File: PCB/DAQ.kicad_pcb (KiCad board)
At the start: 2 copper layers, 6 parts, among them J1 Arduino_Mega_Header, U1 SDshield, U2 RTC, U3 ADC, U4 NOKIA5110, U5 DAC

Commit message: PCB Improvement
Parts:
- added J2: Conn_01x07, Pin_Headers:Pin_Header_Straight_1x07_Pitch2.54mm, F.Cu at (51.7, 27.8)
- added J3: Conn_01x08, Pin_Headers:Pin_Header_Straight_1x08_Pitch2.54mm, F.Cu at (71.9, 27.9)
- added J5: Conn_02x18_Counter_Clockwise, Pin_Headers:Pin_Header_Straight_2x18_Pitch2.54mm, B.Cu at (115.1, 76.1)
- added J6: Conn_01x10, Pin_Headers:Pin_Header_Straight_1x10_Pitch2.54mm, F.Cu at (40.0, 76.2)
- added J7: Conn_01x08, Pin_Headers:Pin_Header_Straight_1x08_Pitch2.54mm, F.Cu at (66.9, 76.1)
- added J8: Conn_01x07, Pin_Headers:Pin_Header_Straight_1x07_Pitch2.54mm, F.Cu at (92.3, 76.2)
- J1, U2: moved to B.Cu
- moved U5 147.7 mm to (35.3, 126.6)
- moved U4 95.8 mm to (65.5, 100.2)
- moved U3 86.6 mm to (26.4, 100.2)
- moved U2 84.3 mm to (128.9, 78.0)
- moved U1 42.0 mm to (127.1, 28.0)
- moved J1 4.92 mm to (70.7, 52.0)

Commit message: PCB Improvements
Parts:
- added C1: 100uF, Capacitors_THT:CP_Axial_L11.0mm_D6.0mm_P18.00mm_Horizontal, F.Cu at (164.2, 112.4)
- added C2: 0.1uF, Capacitors_THT:CP_Axial_L11.0mm_D6.0mm_P18.00mm_Horizontal, F.Cu at (114.6, 113.2)
- added C3: 10uF, Capacitors_THT:CP_Axial_L11.0mm_D6.0mm_P18.00mm_Horizontal, F.Cu at (114.4, 120.6)
- added C4: 1uF, Capacitors_THT:CP_Axial_L11.0mm_D6.0mm_P18.00mm_Horizontal, F.Cu at (114.4, 128.4)
- added CC+1: 0.01uF, Capacitors_THT:CP_Axial_L11.0mm_D6.0mm_P18.00mm_Horizontal, F.Cu at (132.4, 105.0)
- added CC-1: 0.01uF, Capacitors_THT:CP_Axial_L11.0mm_D6.0mm_P18.00mm_Horizontal, F.Cu at (132.4, 135.8)
- added CF+1: 100uF, Capacitors_THT:CP_Axial_L11.0mm_D6.0mm_P18.00mm_Horizontal, F.Cu at (172.6, 105.4)
- added CF-1: 100uF, Capacitors_THT:CP_Axial_L11.0mm_D6.0mm_P18.00mm_Horizontal, F.Cu at (178.4, 136.6)
- added DX+1: D_Schottky, Diodes_THT:D_A-405_P12.70mm_Horizontal, F.Cu at (165.6, 107.0)
- added DX-1: D_Schottky, Diodes_THT:D_A-405_P12.70mm_Horizontal, F.Cu at (158.2, 135.6)
- added IC1: MAX743CWE+, Housings_DIP:DIP-16_W7.62mm, F.Cu at (138.0, 104.6)
- added J4: Conn_01x08, Pin_Headers:Pin_Header_Straight_1x08_Pitch2.54mm, F.Cu at (94.8, 27.8)
- added LX+1: 100uH, Inductors_THT:L_Axial_L9.5mm_D4.0mm_P12.70mm_Horizontal_Fastron_SMCC, F.Cu at (152.8, 87.6)
- added LX-1: 100uH, Inductors_THT:L_Axial_L9.5mm_D4.0mm_P12.70mm_Horizontal_Fastron_SMCC, F.Cu at (152.6, 136.0)
- moved U4 19.6 mm to (54.8, 83.8)
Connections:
- U4 pad 1: /PIN2 -> /PIN7
- U4 pad 2: /PIN3 -> /PIN6
- U4 pad 4: /PIN6 -> /PIN3
- U4 pad 5: /PIN7 -> /PIN2
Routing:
- net /5V: track 0.00 -> 258.3 mm
- net /GND: track 0.00 -> 144.5 mm
- net /3.3V: track 0.00 -> 93.3 mm
- net /PIN4: track 0.00 -> 80.9 mm
- net Net-(C2-Pad1): track 0.00 -> 55.3 mm
- net /SCL: track 0.00 -> 54.8 mm
- net /SDA: track 0.00 -> 52.6 mm
- net /+15V: track 0.00 -> 30.0 mm
- net Net-(DX-1-Pad1): track 0.00 -> 26.4 mm
- net Net-(CC-1-Pad1): track 0.00 -> 15.7 mm
- net Net-(DX+1-Pad2): track 0.00 -> 14.1 mm
- net /PIN35: track 0.00 -> 13.6 mm
- net /PIN31: track 0.00 -> 13.6 mm
- net /PIN33: track 0.00 -> 13.6 mm
- net /PIN6: track 0.00 -> 13.5 mm
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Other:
- net class Default: trace_width 0.25 -> 1

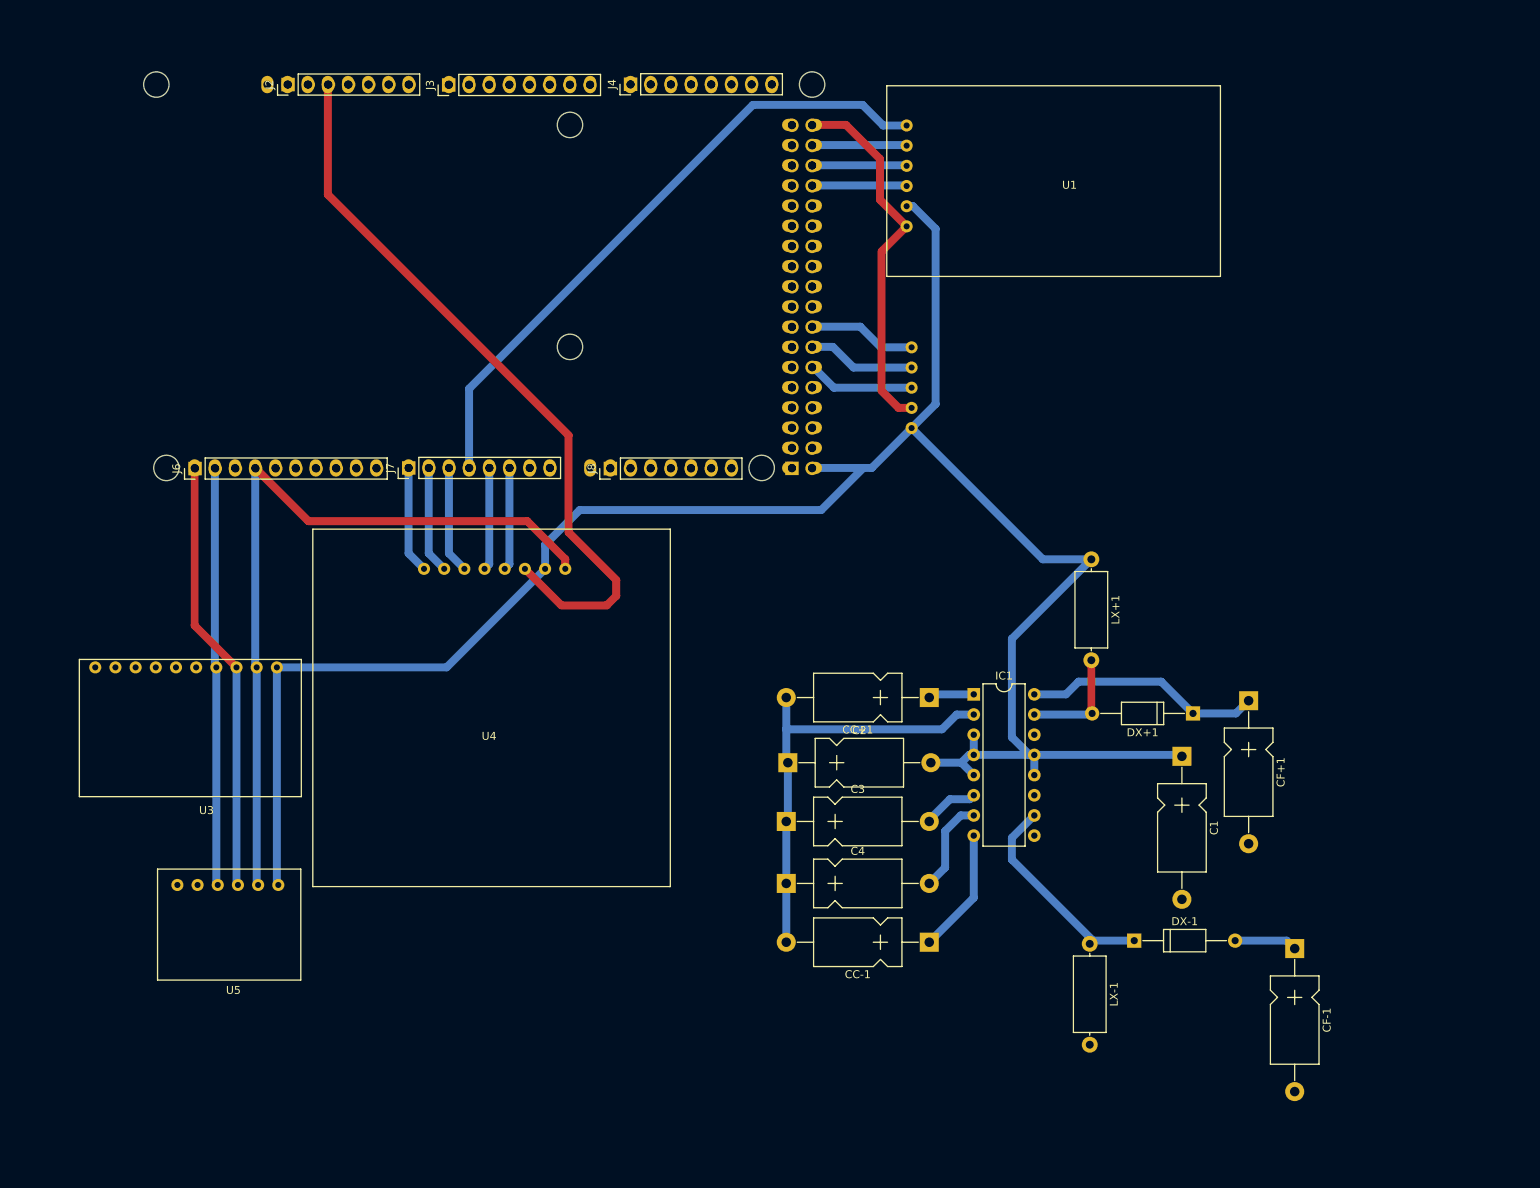
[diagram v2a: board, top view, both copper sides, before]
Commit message: Add ground plane,max743 and started analogic conditioner
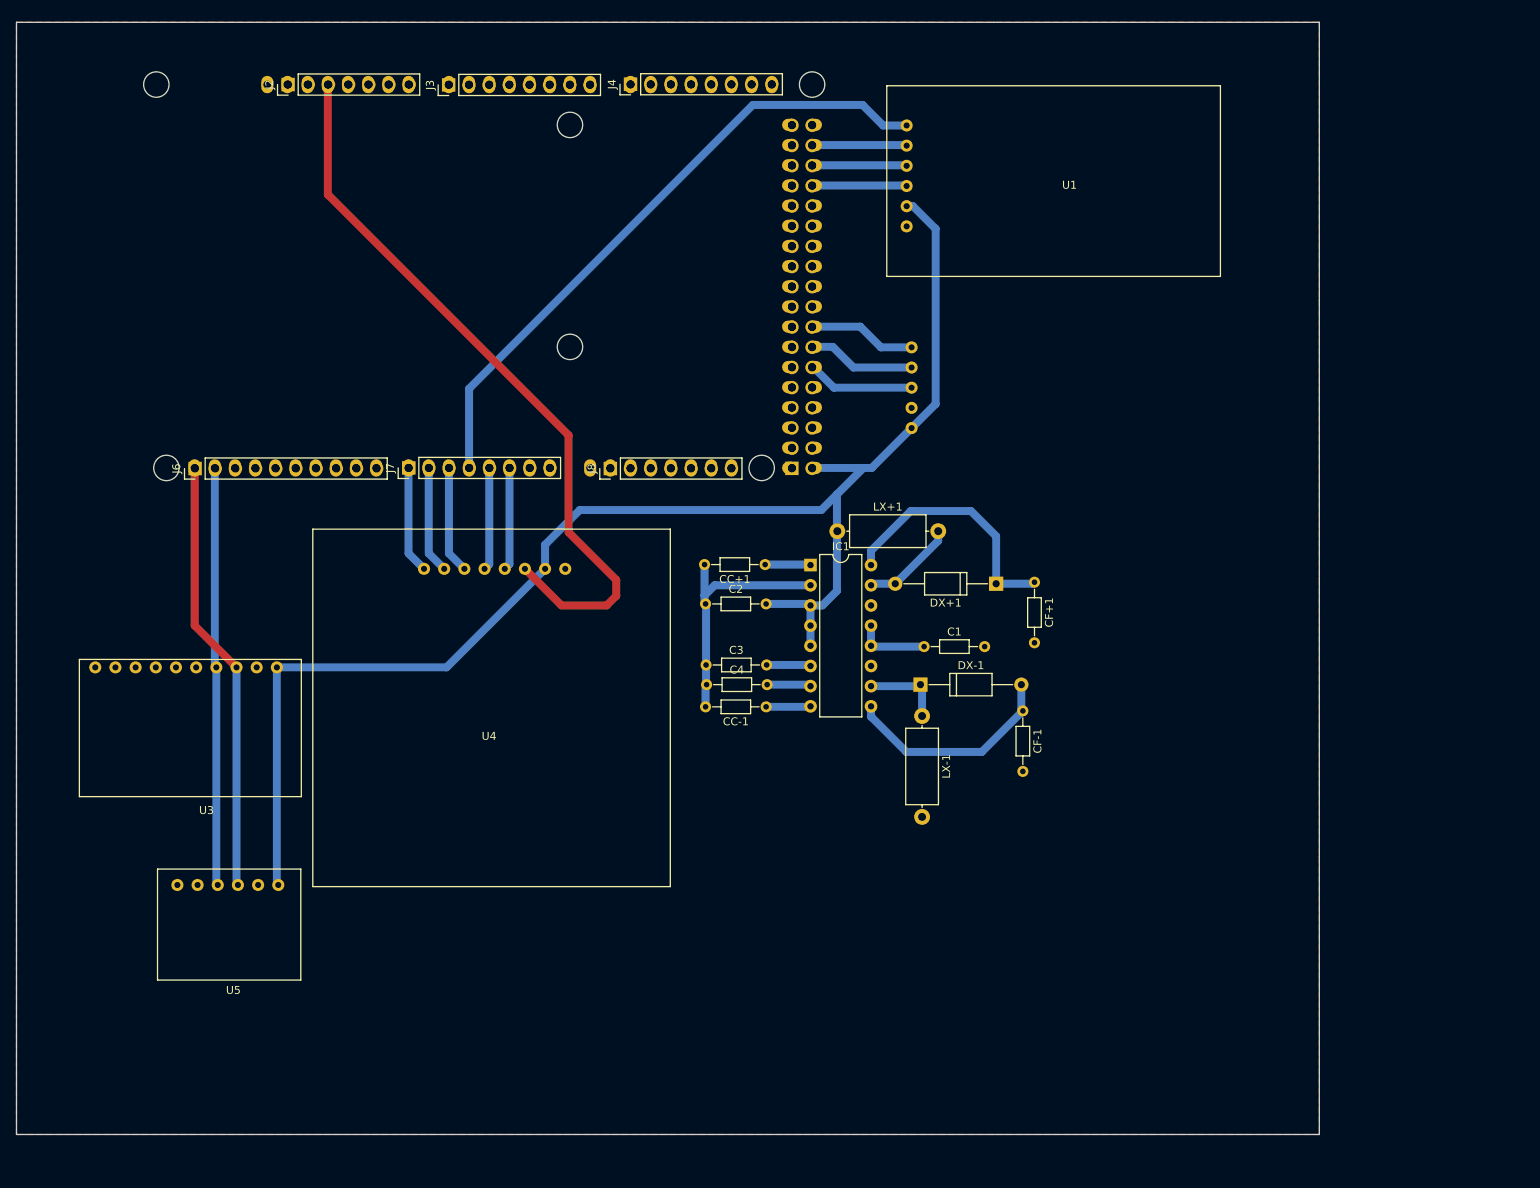
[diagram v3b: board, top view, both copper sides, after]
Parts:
- C1, C2, C3, C4, CC+1, CC-1, CF+1, CF-1: footprint Capacitors_THT:CP_Axial_L11.0mm_D6.0mm_P18.00mm_Horizontal -> Resistors_THT:R_Axial_DIN0204_L3.6mm_D1.6mm_P7.62mm_Horizontal
- moved CF-1 45.5 mm to (144.2, 106.7)
- moved DX-1 42.0 mm to (131.3, 103.4)
- moved CC-1 36.1 mm to (111.9, 106.2)
- moved LX-1 35.6 mm to (131.5, 107.3)
- moved C1 35.3 mm to (131.7, 98.6), turned to 0 degrees
- moved LX+1 32.2 mm to (120.8, 84.1), turned to 0 degrees
- moved CF+1 30.8 mm to (145.6, 90.5)
- moved DX+1 29.7 mm to (140.8, 90.7)
- moved C4 27.0 mm to (104.4, 103.4)
- moved CC+1 26.6 mm to (111.7, 88.3)
- moved IC1 26.2 mm to (117.4, 88.3)
- moved C2 22.5 mm to (104.2, 93.2)
- moved C3 22.1 mm to (104.3, 100.9)
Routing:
- net /GND: track 144.5 -> 0.52 mm
- net /5V: track 258.3 -> 196.1 mm
- net Net-(C2-Pad1): track 55.3 -> 31.9 mm
- net /-15V: track 7.91 -> 27.8 mm
- net Net-(DX-1-Pad1): track 26.4 -> 10.3 mm
- net Net-(CC-1-Pad1): track 15.7 -> 5.61 mm
- net Net-(C4-Pad2): track 11.8 -> 5.54 mm
- net Net-(DX+1-Pad2): track 14.1 -> 12.0 mm
- net /+15V: track 30.0 -> 31.8 mm
- net Net-(C3-Pad2): track 7.08 -> 5.58 mm
- added copper zone on F.Cu, net /GND
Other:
- board outline added: 164 x 140 mm

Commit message: Analog Conditioner added int PCB layout
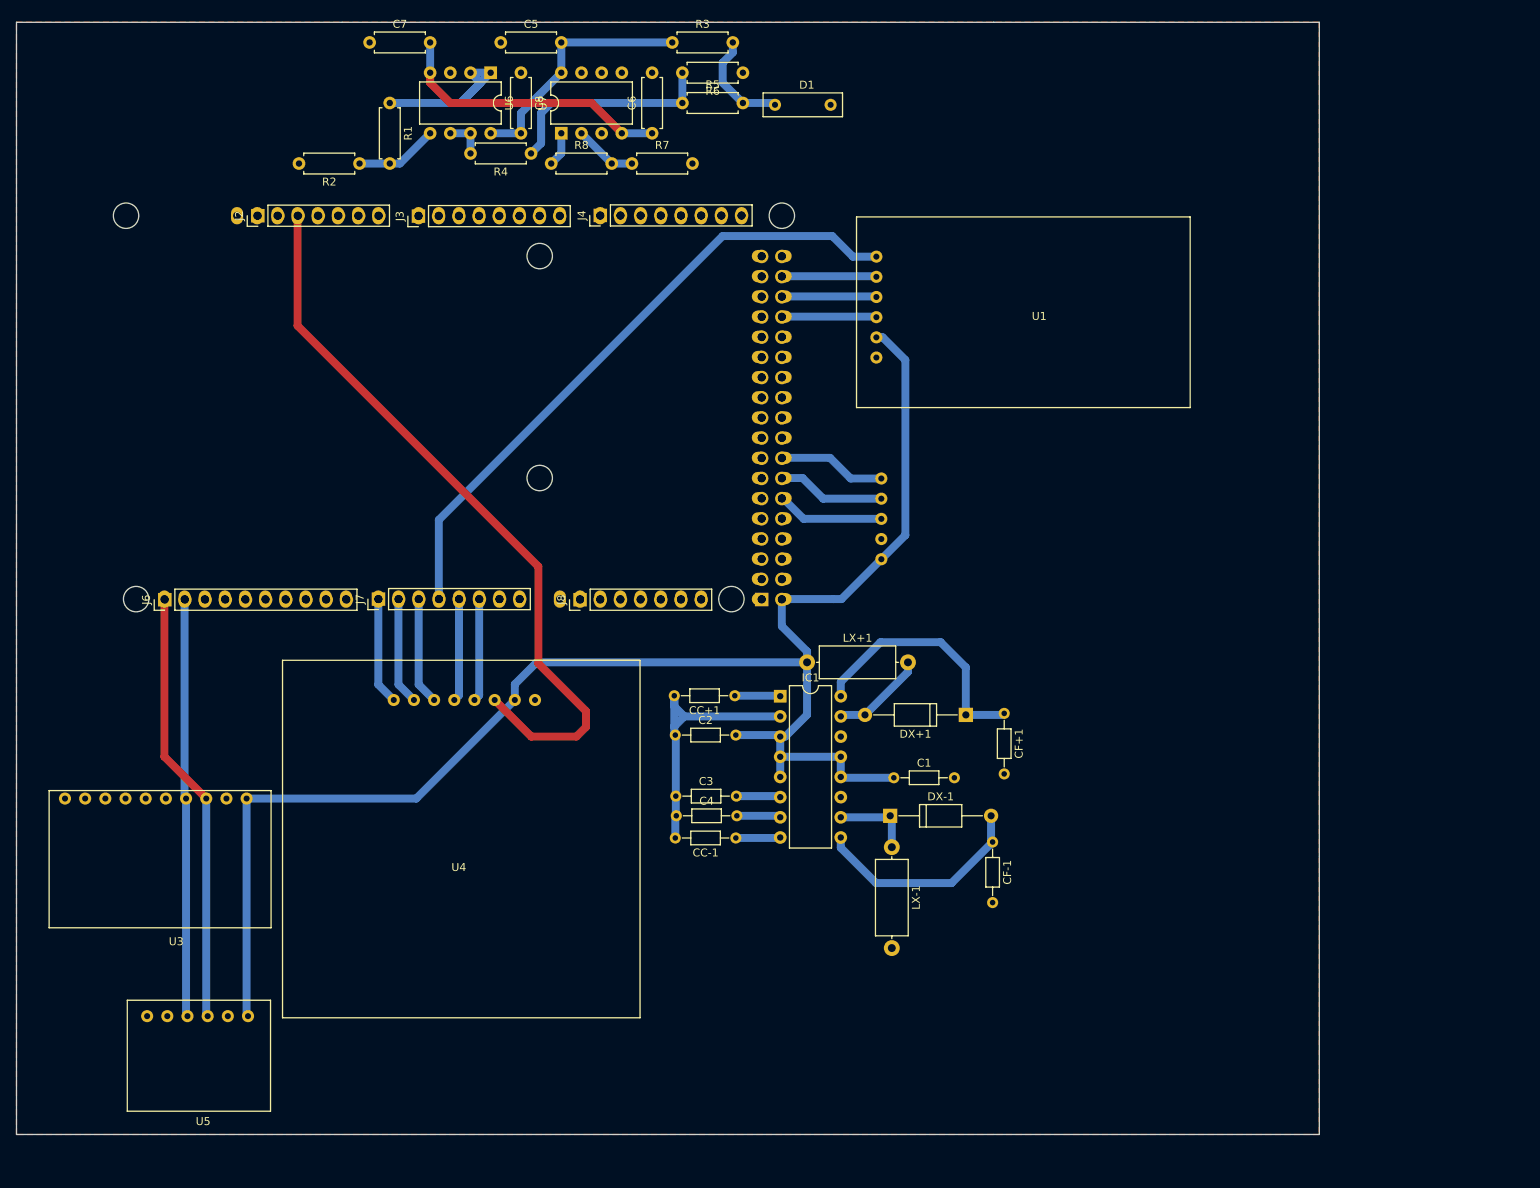
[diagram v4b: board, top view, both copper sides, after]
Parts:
- added C5: 100nF, Resistors_THT:R_Axial_DIN0207_L6.3mm_D2.5mm_P7.62mm_Horizontal, F.Cu at (78.5, 22.5)
- added C6: 100nF, Resistors_THT:R_Axial_DIN0207_L6.3mm_D2.5mm_P7.62mm_Horizontal, F.Cu at (97.5, 34.0)
- added C7: 100nF, Resistors_THT:R_Axial_DIN0207_L6.3mm_D2.5mm_P7.62mm_Horizontal, F.Cu at (62.0, 22.5)
- added C8: 100nF, Resistors_THT:R_Axial_DIN0207_L6.3mm_D2.5mm_P7.62mm_Horizontal, F.Cu at (81.0, 26.4)
- added D1: LM4040, TH-R:R-C-L-D, F.Cu at (111.5, 28.9)
- added R1: 68k, Resistors_THT:R_Axial_DIN0207_L6.3mm_D2.5mm_P7.62mm_Horizontal, F.Cu at (64.5, 30.2)
- added R2: 18k, Resistors_THT:R_Axial_DIN0207_L6.3mm_D2.5mm_P7.62mm_Horizontal, F.Cu at (60.7, 37.8)
- added R3: 22k, Resistors_THT:R_Axial_DIN0207_L6.3mm_D2.5mm_P7.62mm_Horizontal, F.Cu at (100.0, 22.5)
- added R4: 100k, Resistors_THT:R_Axial_DIN0207_L6.3mm_D2.5mm_P7.62mm_Horizontal, F.Cu at (82.3, 36.5)
- added R5: 200k, Resistors_THT:R_Axial_DIN0207_L6.3mm_D2.5mm_P7.62mm_Horizontal, F.Cu at (101.3, 30.2)
- added R6: 51k, Resistors_THT:R_Axial_DIN0207_L6.3mm_D2.5mm_P7.62mm_Horizontal, F.Cu at (108.9, 26.4)
- added R7: 47, Resistors_THT:R_Axial_DIN0207_L6.3mm_D2.5mm_P7.62mm_Horizontal, F.Cu at (95.0, 37.8)
- added R8: 100k, Resistors_THT:R_Axial_DIN0207_L6.3mm_D2.5mm_P7.62mm_Horizontal, F.Cu at (84.8, 37.8)
- added U6: LM358, Housings_DIP:DIP-8_W7.62mm, F.Cu at (77.2, 26.4)
- added U7: LM358, Housings_DIP:DIP-8_W7.62mm, F.Cu at (86.1, 34.0)
- moved LX-1 16.9 mm to (127.7, 123.8)
- moved C1 16.9 mm to (127.9, 115.1)
- moved C3 16.9 mm to (100.5, 117.4)
- moved CC-1 16.9 mm to (108.1, 122.7)
- moved CF+1 16.9 mm to (141.8, 107.0)
- moved CF-1 16.9 mm to (140.4, 123.2)
- moved DX+1 16.9 mm to (137.0, 107.2)
- moved IC1 16.9 mm to (113.6, 104.8)
- moved J7 16.9 mm to (63.1, 92.6)
- moved U2 16.9 mm to (125.1, 94.5)
- moved U5 16.9 mm to (31.4, 143.1)
- moved J3 16.9 mm to (68.1, 44.4)
- moved J4 16.9 mm to (91.0, 44.3)
- moved J5 16.9 mm to (111.3, 92.7)
- moved J6 16.9 mm to (36.2, 92.7)
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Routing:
- net /-15V: track 27.8 -> 63.4 mm
- net /15V: track 0.00 -> 31.3 mm
- net Net-(R4-Pad1): track 0.00 -> 27.7 mm
- net Net-(R1-Pad1): track 0.00 -> 22.2 mm
- net Net-(D1-Pad1): track 0.00 -> 13.3 mm
- net Net-(R1-Pad2): track 0.00 -> 10.5 mm
- net Net-(R7-Pad1): track 0.00 -> 7.93 mm
- net Net-(R4-Pad2): track 0.00 -> 5.08 mm
- net /5V: track 196.1 -> 200.7 mm
- net Net-(R8-Pad1): track 0.00 -> 4.34 mm
- net Net-(C2-Pad1): track 31.9 -> 35.0 mm

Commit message: Changed RTC module on PCB
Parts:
- U2: footprint RTC:SDShield -> SDShield:SDShield; moved to F.Cu
- U4: moved to B.Cu
- moved U4 45.4 mm to (96.2, 103.8), turned to 180 degrees
- moved U2 25.1 mm to (122.9, 69.5)
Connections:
- J1 pad 26: Net-(J1-Pad26) -> /PIN52
- J1 pad 27: Net-(J1-Pad27) -> /PIN50
- J1 pad 43: /GND -> Net-(J1-Pad43)
- J1 pad 44: /PIN52 -> /PIN53
- J1 pad 46: /PIN50 -> Net-(J1-Pad46)
- J1 pad 71: /PIN2 -> Net-(J1-Pad71)
- J8 pad 6: Net-(J8-Pad6) -> /SDA
- J8 pad 7: Net-(J8-Pad7) -> /SCL
- U1 pad 1: /PIN4 -> /PIN53
- U2 pad 1: /5V -> /GND
- U2 pad 2: /GND -> /5V
- U2 pad 3: /PIN31 -> /SDA
- U2 pad 4: /PIN33 -> /SCL
- U2 pad 5: /PIN35 -> (no net)
- U4 pad 1: /PIN7 -> /PIN3
- U4 pad 2: /PIN6 -> /PIN4
- U4 pad 4: /PIN3 -> /PIN6
- U4 pad 5: /PIN2 -> /PIN7
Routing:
- net /PIN4: track 80.9 -> 20.0 mm
- net /5V: track 200.7 -> 233.1 mm
- net /3.3V: track 93.3 -> 71.4 mm
- net /PIN33: track 13.6 -> 0.00 mm
- net /PIN35: track 13.6 -> 0.00 mm
- net /PIN31: track 13.6 -> 0.15 mm
- net /PIN2: track 12.9 -> 0.00 mm
- net /PIN53: track 0.00 -> 11.8 mm
- net /PIN52: track 11.9 -> 0.10 mm
- net /PIN50: track 11.9 -> 0.10 mm
- net /PIN3: track 12.9 -> 20.0 mm
- net /PIN7: track 13.5 -> 20.0 mm
- net /PIN6: track 13.5 -> 20.0 mm
- net /PIN5: track 13.5 -> 20.0 mm

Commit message: Improvements on the PCB
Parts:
- added J10: Conn_01x01, Pin_Headers:Pin_Header_Straight_1x01_Pitch2.54mm, F.Cu at (120.9, 52.0)
- added J11: Conn_01x01, Pin_Headers:Pin_Header_Straight_1x01_Pitch2.54mm, F.Cu at (106.4, 54.7)
- added J12: Conn_01x01, Pin_Headers:Pin_Header_Straight_1x01_Pitch2.54mm, F.Cu at (103.7, 50.7)
- added J9: Conn_01x01, Pin_Headers:Pin_Header_Straight_1x01_Pitch2.54mm, F.Cu at (103.2, 54.4)
- moved J8 0.12 mm to (88.3, 92.6)
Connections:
- J1 pad 61: Net-(J1-Pad61) -> /SCL
- J1 pad 62: Net-(J1-Pad62) -> /SDA
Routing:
- net /SDA: track 52.6 -> 94.0 mm, vias 0 -> 2
- net /PIN52: track 0.10 -> 41.2 mm
- net /SCL: track 54.8 -> 94.1 mm, vias 0 -> 1
- net /PIN50: track 0.10 -> 30.9 mm
- net /5V: track 233.1 -> 253.0 mm
- net Net-(J5-Pad31): track 0.00 -> 5.10 mm
- net Net-(J5-Pad33): track 0.00 -> 5.09 mm
- net /PIN53: track 11.8 -> 7.16 mm
